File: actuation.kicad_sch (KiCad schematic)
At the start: 19 parts

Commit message: Reorganizing schematic
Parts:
- added C? (x2): 1uF, Capacitor_SMD:C_0603_1608Metric, symbol Device:C_Small
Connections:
- net +3.3V: now also C?.1, C?.1
- net GND: now also C?.2, C?.2
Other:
- note added: "Interfacing (COLD)"
- note added: "Power Supply (COLD)"
- note added: "Subsheets"
- moved on the sheet: C?, U?

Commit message: More reorganizing
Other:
- note added: "Cold-side Power Supply"
- note added: "Interfacing"
- note removed: "Interfacing (COLD)"
- note removed: "Power Supply (COLD)"
- moved on the sheet: J?, R?

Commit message: Terminal block part selections
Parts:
- J?: footprint interface:182-009-213R561 -> actuation:182-009-213R561
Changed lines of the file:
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@@
       (effects (font (size 1.27 1.27)) (justify left))
     )
-    (property "Footprint" "interface:182-009-213R561" (id 2) (at 50.8 46.99 0)
+    (property "Footprint" "actuation:182-009-213R561" (id 2) (at 50.8 46.99 0)
       (effects (font (size 1.27 1.27)) hide)
     )
@@
       (reference "J?") (unit 1) (value "ACT CH2") (footprint "TerminalBlock_Phoenix:TerminalBlock_Phoenix_PT-1,5-2-5.0-H_1x02_P5.00mm_Horizontal")
     )
-    (path "/2330c4d7-2ab7-4b99-8e5d-6a68e3c59825/10c4a3b2-adeb-45cc-a7d6-3806d9063cb2"
-      (reference "J?") (unit 1) (value "FB CH2") (footprint "")
+    (path "/6d7df23a-0810-4327-8a09-0091cb17fdd4/152548fa-3aa6-446f-8c00-d4ce48581397"
+      (reference "J?") (unit 1) (value "ENERGIZE") (footprint "TerminalBlock_Phoenix:TerminalBlock_Phoenix_PT-1,5-2-5.0-H_1x02_P5.00mm_Horizontal")
     )
     (path "/fb8ad72d-4567-40d4-a185-735199b25125/1599112a-dd2b-4c99-b32d-fd074d29b607"
@@
       (reference "J?") (unit 1) (value "FB CH1") (footprint "")
     )
-    (path "/2330c4d7-2ab7-4b99-8e5d-6a68e3c59825/1db1a5bd-7244-407c-bbd2-fd885397bacc"
-      (reference "J?") (unit 1) (value "FB CH3") (footprint "")
+    (path "/2330c4d7-2ab7-4b99-8e5d-6a68e3c59825/1c7e212c-734c-4de6-8136-e158a3794bc4"
+      (reference "J?") (unit 1) (value "FB CH4") (footprint "")
     )
     (path "/fb8ad72d-4567-40d4-a185-735199b25125/222876db-7cf3-48a9-8dd1-016cb0b793fd"
@@
     )
     (path "/73a2f7f3-4823-454a-bfba-81a74cbf18fe"
-      (reference "J?") (unit 1) (value "ACTUATION") (footprint "interface:182-009-213R561")
+      (reference "J?") (unit 1) (value "ACTUATION") (footprint "actuation:182-009-213R561")
+    )
+    (path "/2330c4d7-2ab7-4b99-8e5d-6a68e3c59825/75716198-79c0-43b9-84ec-8a4194eed539"
+      (reference "J?") (unit 1) (value "FB CH2") (footprint "")
     )
     (path "/fb8ad72d-4567-40d4-a185-735199b25125/8a11a001-07f6-4a81-9b77-ffcef3553d19"
       (reference "J?") (unit 1) (value "ACT CH4") (footprint "TerminalBlock_Phoenix:TerminalBlock_Phoenix_PT-1,5-2-5.0-H_1x02_P5.00mm_Horizontal")
     )
-    (path "/2330c4d7-2ab7-4b99-8e5d-6a68e3c59825/8d534225-4c22-4603-9f54-7fa1660546c6"
-      (reference "J?") (unit 1) (value "FB CH4") (footprint "")
-    )
     (path "/fb8ad72d-4567-40d4-a185-735199b25125/947c2909-e8bb-414b-b22f-a25c39fc9a50"
       (reference "J?") (unit 1) (value "ACT CH9") (footprint "TerminalBlock_Phoenix:TerminalBlock_Phoenix_PT-1,5-2-5.0-H_1x02_P5.00mm_Horizontal")
@@
       (reference "J?") (unit 1) (value "ACT CH10") (footprint "TerminalBlock_Phoenix:TerminalBlock_Phoenix_PT-1,5-2-5.0-H_1x02_P5.00mm_Horizontal")
     )
+    (path "/2330c4d7-2ab7-4b99-8e5d-6a68e3c59825/9ae8adc9-aff6-4790-a583-7a7ba48ce076"
+      (reference "J?") (unit 1) (value "FB CH3") (footprint "")
+    )
     (path "/fb8ad72d-4567-40d4-a185-735199b25125/9f1f7c18-0b54-45ea-948d-192c45d7436c"
       (reference "J?") (unit 1) (value "ACT CH1") (footprint "TerminalBlock_Phoenix:TerminalBlock_Phoenix_PT-1,5-2-5.0-H_1x02_P5.00mm_Horizontal")
@@
       (reference "J?") (unit 1) (value "ACT CH6") (footprint "TerminalBlock_Phoenix:TerminalBlock_Phoenix_PT-1,5-2-5.0-H_1x02_P5.00mm_Horizontal")
     )
-    (path "/6d7df23a-0810-4327-8a09-0091cb17fdd4/b5c29e46-abad-49b2-8998-a24d63385889"
-      (reference "J?") (unit 1) (value "ACT ARMED") (footprint "")
-    )
-    (path "/6d7df23a-0810-4327-8a09-0091cb17fdd4/b5f8a875-1e16-4124-b5ce-87193df399ee"
-      (reference "J?") (unit 1) (value "ACT DISARMED") (footprint "")
-    )
-    (path "/6d7df23a-0810-4327-8a09-0091cb17fdd4/bf961f8c-33c7-4f8f-96a9-ad7ced2de25d"
-      (reference "J?") (unit 1) (value "ENERGIZE") (footprint "")
+    (path "/6d7df23a-0810-4327-8a09-0091cb17fdd4/c8f0799d-64bf-4127-a02b-49a2765b5f8f"
+      (reference "J?") (unit 1) (value "ACT ARMED") (footprint "TerminalBlock_Phoenix:TerminalBlock_Phoenix_PT-1,5-2-5.0-H_1x02_P5.00mm_Horizontal")
     )
     (path "/fb8ad72d-4567-40d4-a185-735199b25125/f421939d-f41b-4677-be07-4ac7167b129d"
       (reference "J?") (unit 1) (value "ACT CH5") (footprint "TerminalBlock_Phoenix:TerminalBlock_Phoenix_PT-1,5-2-5.0-H_1x02_P5.00mm_Horizontal")
     )
+    (path "/6d7df23a-0810-4327-8a09-0091cb17fdd4/f7c90e1b-29df-4b03-8cc2-eddba8f49b87"
+      (reference "J?") (unit 1) (value "ACT DISARMED") (footprint "TerminalBlock_Phoenix:TerminalBlock_Phoenix_PT-1,5-2-5.0-H_1x02_P5.00mm_Horizontal")
+    )
     (path "/6d7df23a-0810-4327-8a09-0091cb17fdd4/3289038b-8941-4b8f-a3ce-d0287a5ba46b"

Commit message: more notes, generate pdf
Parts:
- gave numbers to parts that had none: 21
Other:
- note added: "600Ω and 120Ω as recommended by the datasheet for CAT5 (100Ω)"
- note added: "I2C addresses: Actuator GPIO 1-8: 0x20 Actuator GPIO 9-16: 0x21 Feedback GPIO: 0x23 Current sense ADC: 0x48-0x4F"

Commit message: notes on feedback sheet
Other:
- note added: "500mA output"
- note added: "Only ground the DSUB on one side, probably ground it at the C&C"
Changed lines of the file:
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@@
     (stroke (width 0) (type default) (color 0 0 0 0))
+  )
+  (text "500mA output" (at 237.49 17.78 0)
+    (effects (font (size 1.27 1.27)) (justify left bottom))
   )
   (text "Interfacing" (at 17.78 102.87 0)
@@
     (effects (font (size 1.27 1.27)) (justify left bottom))
   )
+  (text "Only ground the DSUB on one side, \nprobably ground it at the C&C"
+    (at 38.1 71.12 0)
+    (effects (font (size 1.27 1.27)) (justify left bottom))
+  )

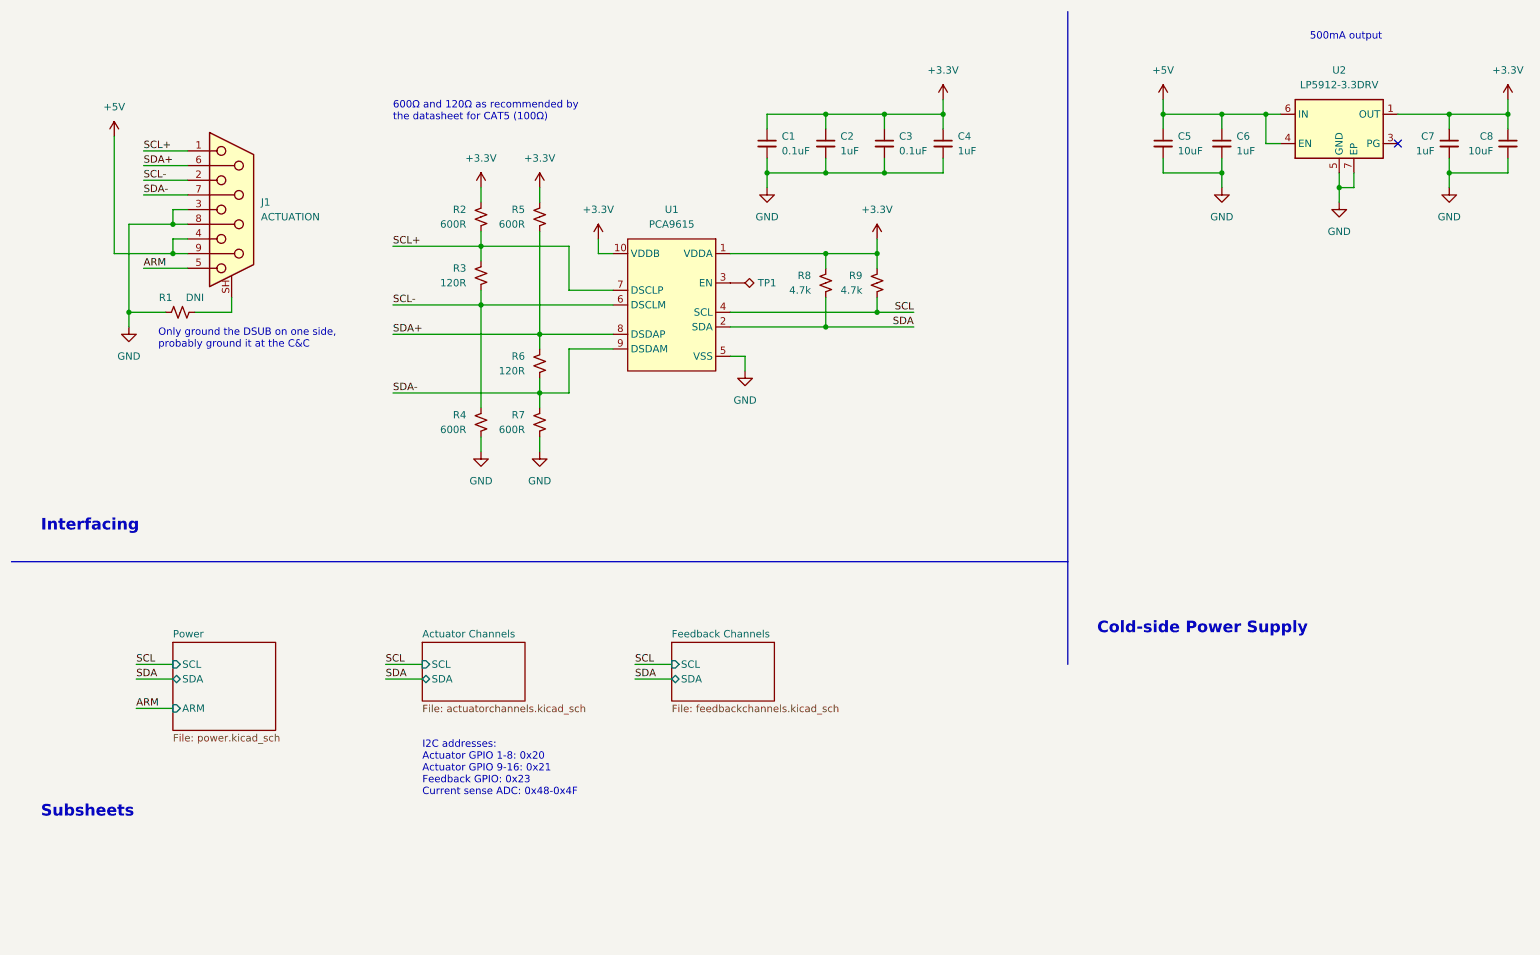
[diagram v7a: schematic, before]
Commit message: estimate 3.3V current consumption
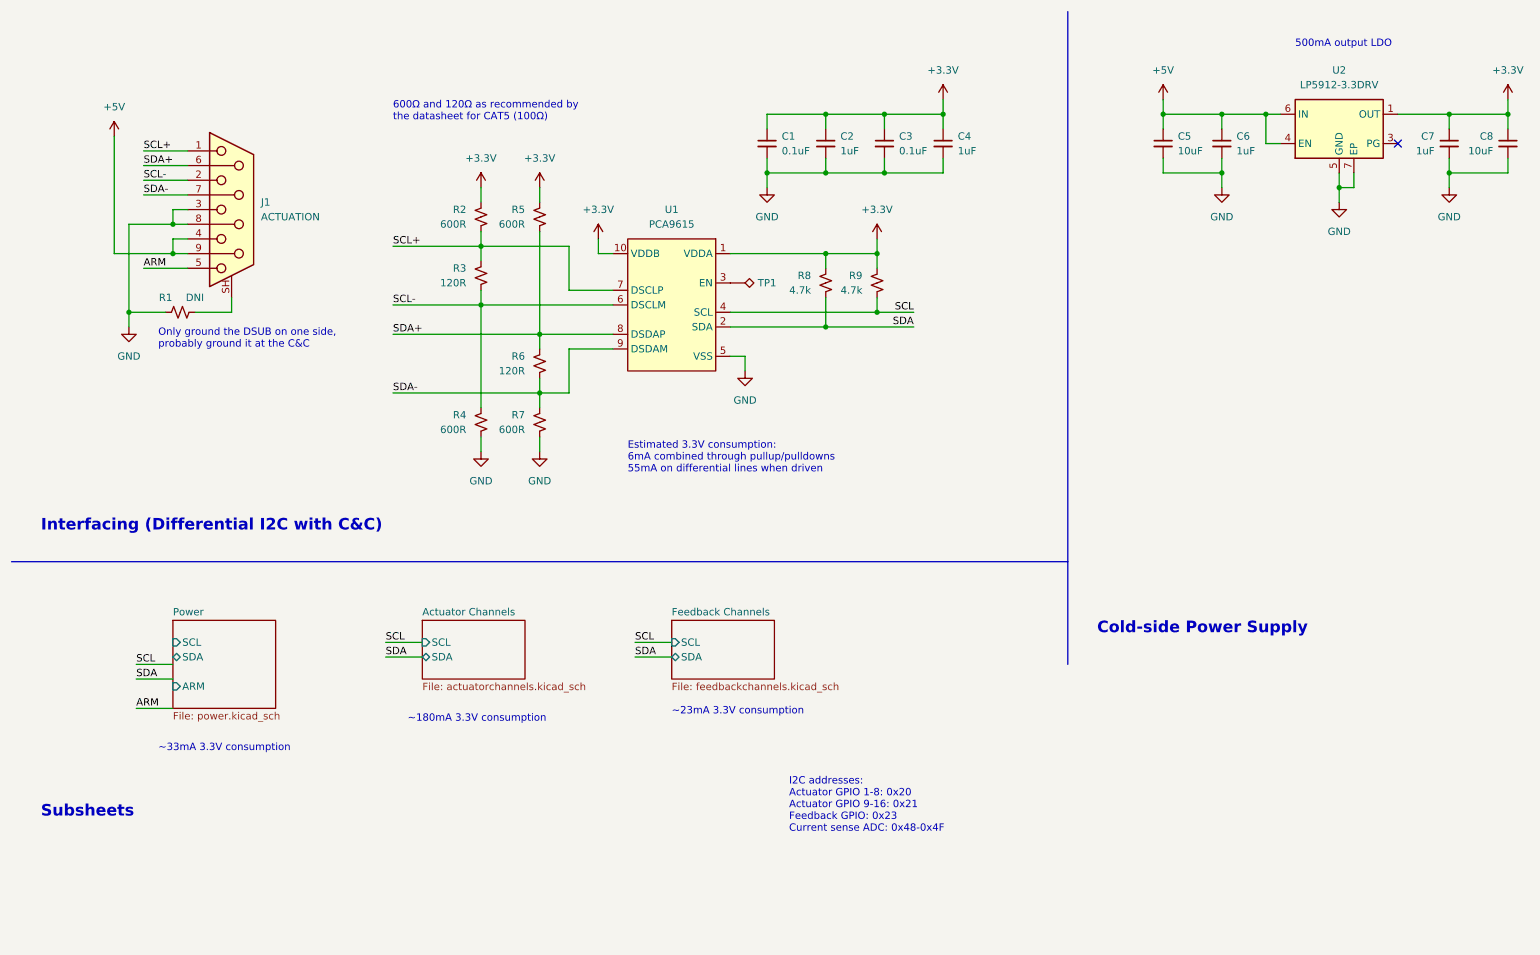
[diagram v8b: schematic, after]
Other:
- note added: "500mA output LDO"
- note added: "Estimated 3.3V consumption: 6mA combined through pullup/pulldowns 55mA on differential lines when driven"
- note added: "Interfacing (Differential I2C with C&C)"
- note added: "~180mA 3.3V consumption"
- note added: "~23mA 3.3V consumption"
- note added: "~33mA 3.3V consumption"
- note removed: "500mA output"
- note removed: "Interfacing"
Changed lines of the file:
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@@
     (stroke (width 0) (type default) (color 0 0 0 0))
   )
-  (wire (pts (xy 77.47 128.27) (xy 83.82 128.27))
+  (wire (pts (xy 77.47 124.46) (xy 83.82 124.46))
     (stroke (width 0) (type default) (color 0 0 0 0))
   )
@@
     (stroke (width 0) (type default) (color 0 0 0 0))
   )
-  (wire (pts (xy 120.65 125.73) (xy 127 125.73))
+  (wire (pts (xy 120.65 121.92) (xy 127 121.92))
     (stroke (width 0) (type default) (color 0 0 0 0))
   )
@@
     (stroke (width 0) (type default) (color 0 0 0 0))
   )
-  (wire (pts (xy 120.65 128.27) (xy 127 128.27))
+  (wire (pts (xy 120.65 124.46) (xy 127 124.46))
     (stroke (width 0) (type default) (color 0 0 0 0))
   )
@@
     (stroke (width 0) (type default) (color 0 0 0 0))
   )
-  (wire (pts (xy 77.47 125.73) (xy 83.82 125.73))
+  (wire (pts (xy 77.47 121.92) (xy 83.82 121.92))
     (stroke (width 0) (type default) (color 0 0 0 0))
   )
@@
     (stroke (width 0) (type default) (color 0 0 0 0))
   )
-  (text "500mA output" (at 237.49 17.78 0)
-    (effects (font (size 1.27 1.27)) (justify left bottom))
-  )
-  (text "Interfacing" (at 17.78 102.87 0)
+  (text "~180mA 3.3V consumption" (at 81.28 135.89 0)
+    (effects (font (size 1.27 1.27)) (justify left bottom))
+  )
+  (text "500mA output LDO" (at 234.95 19.05 0)
+    (effects (font (size 1.27 1.27)) (justify left bottom))
+  )
+  (text "Interfacing (Differential I2C with C&C)" (at 17.78 102.87 0)
     (effects (font (size 2 2) bold) (justify left bottom))
   )
@@
     (effects (font (size 1.27 1.27)) (justify left bottom))
   )
+  (text "~23mA 3.3V consumption\n" (at 127 134.62 0)
+    (effects (font (size 1.27 1.27)) (justify left bottom))
+  )
   (text "Only ground the DSUB on one side, \nprobably ground it at the C&C"
     (at 38.1 71.12 0)
@@
   )
   (text "I2C addresses:\nActuator GPIO 1-8: 0x20\nActuator GPIO 9-16: 0x21\nFeedback GPIO: 0x23 \nCurrent sense ADC: 0x48-0x4F"
-    (at 83.82 148.59 0)
+    (at 147.32 154.94 0)
+    (effects (font (size 1.27 1.27)) (justify left bottom))
+  )
+  (text "~33mA 3.3V consumption" (at 38.1 140.97 0)
     (effects (font (size 1.27 1.27)) (justify left bottom))
   )
@@
     (effects (font (size 2 2) bold) (justify left bottom))
   )
+  (text "Estimated 3.3V consumption:\n6mA combined through pullup/pulldowns\n55mA on differential lines when driven"
+    (at 119.38 92.71 0)
+    (effects (font (size 1.27 1.27)) (justify left bottom))
+  )
   (label "SCL+" (at 35.56 36.83 0)
     (effects (font (size 1.27 1.27)) (justify left bottom))
@@
     (effects (font (size 1.27 1.27)) (justify left bottom))
   )
-  (label "SCL" (at 120.65 125.73 0)
+  (label "SCL" (at 120.65 121.92 0)
     (effects (font (size 1.27 1.27)) (justify left bottom))
   )
@@
     (effects (font (size 1.27 1.27)) (justify right bottom))
   )
-  (label "SCL" (at 77.47 125.73 0)
+  (label "SCL" (at 77.47 121.92 0)
     (effects (font (size 1.27 1.27)) (justify left bottom))
   )
@@
     (effects (font (size 1.27 1.27)) (justify left bottom))
   )
-  (label "SDA" (at 77.47 128.27 0)
+  (label "SDA" (at 77.47 124.46 0)
     (effects (font (size 1.27 1.27)) (justify left bottom))
   )
@@
     (effects (font (size 1.27 1.27)) (justify right bottom))
   )
-  (label "SDA" (at 120.65 128.27 0)
+  (label "SDA" (at 120.65 124.46 0)
     (effects (font (size 1.27 1.27)) (justify left bottom))
   )
@@
     (pin "2")
   )
-  (sheet (at 127 121.92) (size 17.78 10.16) (fields_autoplaced)
+  (sheet (at 127 118.11) (size 17.78 10.16) (fields_autoplaced)
     (stroke (width 0.1524) (type solid) (color 0 0 0 0))
     (fill (color 0 0 0 0.0000))
-    (property "Sheet name" "Feedback Channels" (id 0) (at 127 121.2084 0)
+    (property "Sheet name" "Feedback Channels" (id 0) (at 127 117.3984 0)
       (effects (font (size 1.27 1.27)) (justify left bottom))
     )
-    (property "Sheet file" "feedbackchannels.kicad_sch" (id 1) (at 127 132.6646 0)
+    (property "Sheet file" "feedbackchannels.kicad_sch" (id 1) (at 127 128.8546 0)
       (effects (font (size 1.27 1.27)) (justify left top))
     )
-    (pin "SCL" input (at 127 125.73 180)
-      (effects (font (size 1.27 1.27)) (justify left))
-    )
-    (pin "SDA" bidirectional (at 127 128.27 180)
-      (effects (font (size 1.27 1.27)) (justify left))
-    )
-  )
-  (sheet (at 40.64 121.92) (size 17.78 15.24) (fields_autoplaced)
+    (pin "SCL" input (at 127 121.92 180)
+      (effects (font (size 1.27 1.27)) (justify left))
+    )
+    (pin "SDA" bidirectional (at 127 124.46 180)
+      (effects (font (size 1.27 1.27)) (justify left))
+    )
+  )
+  (sheet (at 40.64 118.11) (size 17.78 15.24) (fields_autoplaced)
     (stroke (width 0.1524) (type solid) (color 0 0 0 0))
     (fill (color 0 0 0 0.0000))
-    (property "Sheet name" "Power" (id 0) (at 40.64 121.2084 0)
+    (property "Sheet name" "Power" (id 0) (at 40.64 117.3984 0)
       (effects (font (size 1.27 1.27)) (justify left bottom))
     )
-    (property "Sheet file" "power.kicad_sch" (id 1) (at 40.64 137.7446 0)
+    (property "Sheet file" "power.kicad_sch" (id 1) (at 40.64 133.9346 0)
       (effects (font (size 1.27 1.27)) (justify left top))
     )
-    (pin "SCL" input (at 40.64 125.73 180)
-      (effects (font (size 1.27 1.27)) (justify left))
-    )
-    (pin "SDA" bidirectional (at 40.64 128.27 180)
-      (effects (font (size 1.27 1.27)) (justify left))
-    )
-    (pin "ARM" input (at 40.64 133.35 180)
-      (effects (font (size 1.27 1.27)) (justify left))
-    )
-  )
-  (sheet (at 83.82 121.92) (size 17.78 10.16) (fields_autoplaced)
+    (pin "SCL" input (at 40.64 121.92 180)
+      (effects (font (size 1.27 1.27)) (justify left))
+    )
+    (pin "SDA" bidirectional (at 40.64 124.46 180)
+      (effects (font (size 1.27 1.27)) (justify left))
+    )
+    (pin "ARM" input (at 40.64 129.54 180)
+      (effects (font (size 1.27 1.27)) (justify left))
+    )
+  )
+  (sheet (at 83.82 118.11) (size 17.78 10.16) (fields_autoplaced)
     (stroke (width 0.1524) (type solid) (color 0 0 0 0))
     (fill (color 0 0 0 0.0000))
-    (property "Sheet name" "Actuator Channels" (id 0) (at 83.82 121.2084 0)
+    (property "Sheet name" "Actuator Channels" (id 0) (at 83.82 117.3984 0)
       (effects (font (size 1.27 1.27)) (justify left bottom))
     )
-    (property "Sheet file" "actuatorchannels.kicad_sch" (id 1) (at 83.82 132.6646 0)
+    (property "Sheet file" "actuatorchannels.kicad_sch" (id 1) (at 83.82 128.8546 0)
       (effects (font (size 1.27 1.27)) (justify left top))
     )
-    (pin "SDA" bidirectional (at 83.82 128.27 180)
-      (effects (font (size 1.27 1.27)) (justify left))
-    )
-    (pin "SCL" input (at 83.82 125.73 180)
-      (effects (font (size 1.27 1.27)) (justify left))
-    )
+    (pin "SDA" bidirectional (at 83.82 124.46 180)
+      (effects (font (size 1.27 1.27)) (justify left))
+    )
+    (pin "SCL" input (at 83.82 121.92 180)
+      (effects (font (size 1.27 1.27)) (justify left))
+    )
